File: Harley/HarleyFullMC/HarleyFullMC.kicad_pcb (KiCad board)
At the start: 10 copper layers, 33 x 45 mm, 214 parts, among them J1 USB_3.1_microB, J3 CONN_01X04, J4 CONN_02X05, J5 DF40C_60DP_0-4V, J6 CONN_01X06, U1 xc7a50tcsg324pkg, U10 LTM4622, U11 OSCILLATOR, U12 24LC128T-I/MNY, U2 LTM4622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

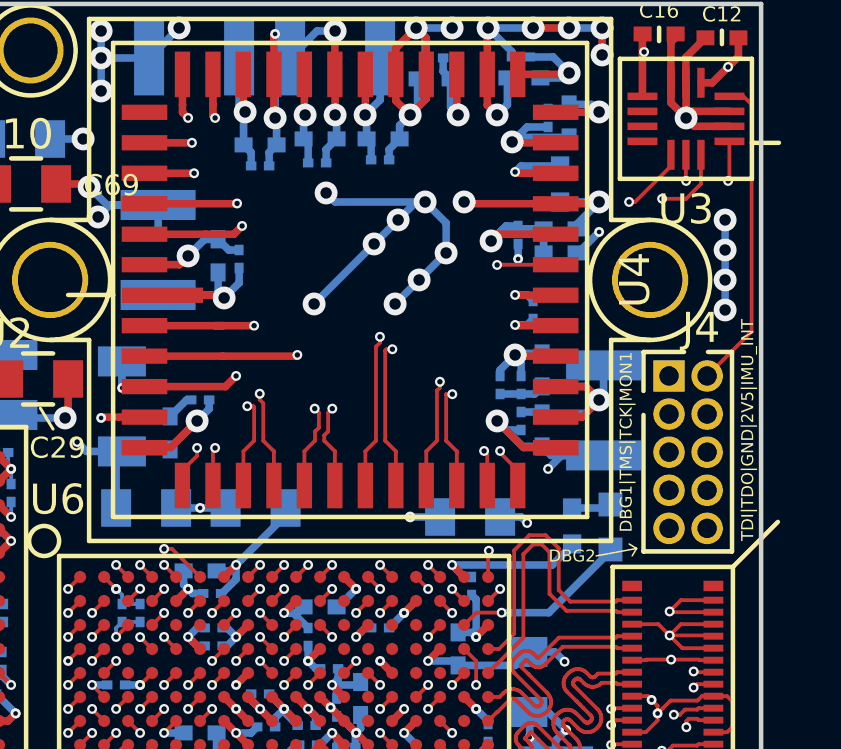
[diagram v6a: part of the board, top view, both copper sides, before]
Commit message: fixed no net vias under imager chip
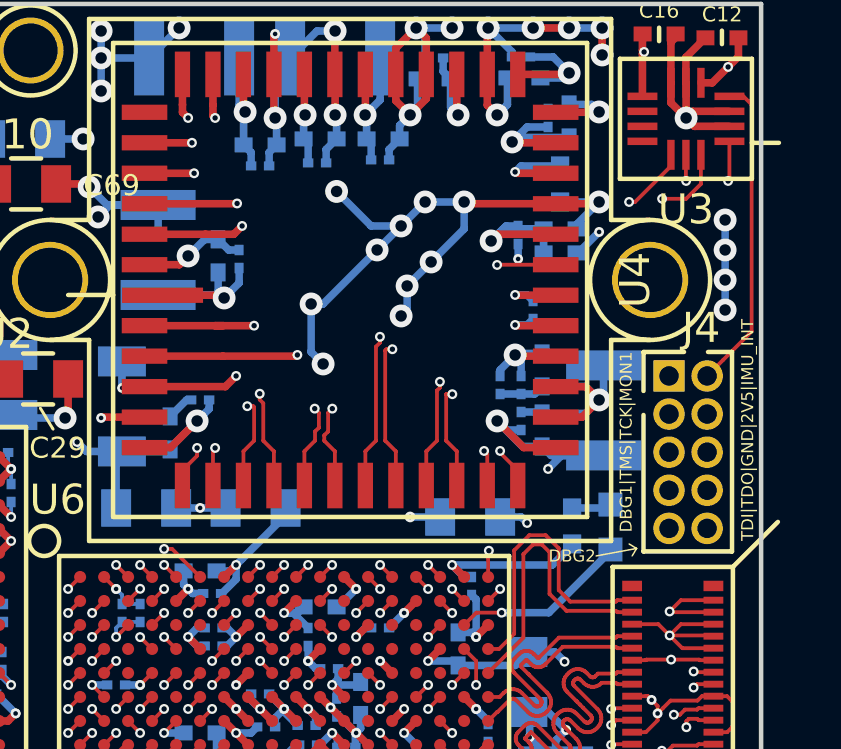
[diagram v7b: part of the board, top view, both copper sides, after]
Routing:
- net GND: track 350.2 -> 366.2 mm, vias 202 -> 211
- net (no net): track 15.9 -> 3.00 mm, vias 14 -> 6
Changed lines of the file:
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@@
     (links 864)
     (no_connects 0)
-    (area 11.924999 152.924999 45.075001 198.075001)
+    (area 8.286961 149.048 50.487715 201.885333)
     (thickness 1.6)
     (drawings 66)
-    (tracks 6054)
+    (tracks 6059)
     (zones 0)
     (modules 214)
@@
   (page A4)
   (layers
-    (0 F.Cu signal hide)
-    (1 In1.Cu power hide)
-    (2 In2.Cu signal hide)
-    (3 In3.Cu signal hide)
-    (4 In4.Cu power hide)
-    (5 In5.Cu signal hide)
-    (6 In6.Cu power hide)
-    (7 In7.Cu power hide)
-    (8 In8.Cu power hide)
+    (0 F.Cu signal)
+    (1 In1.Cu power)
+    (2 In2.Cu signal)
+    (3 In3.Cu signal)
+    (4 In4.Cu power)
+    (5 In5.Cu signal)
+    (6 In6.Cu power)
+    (7 In7.Cu power)
+    (8 In8.Cu power)
     (31 B.Cu signal)
     (34 B.Paste user hide)
@@
   )
   (setup
-    (last_trace_width 0.127)
+    (last_trace_width 0.254)
     (user_trace_width 0.127)
     (user_trace_width 0.254)
@@
     (tags "capacitor 0402")
     (attr smd)
-    (fp_text reference C10 (at 0 1.4) (layer B.SilkS)
+    (fp_text reference C10 (at -0.3 1.7) (layer B.SilkS)
       (effects (font (size 0.5 0.5) (thickness 0.07)) (justify mirror))
     )
@@
     (tags "capacitor 0201")
     (attr smd)
-    (fp_text reference C32 (at 0.05 1.5) (layer B.SilkS)
+    (fp_text reference C32 (at -0.2 1.7) (layer B.SilkS)
       (effects (font (size 0.5 0.5) (thickness 0.07)) (justify mirror))
     )
@@
     (effects (font (size 0.4 0.4) (thickness 0.06)) (justify mirror))
   )
-  (gr_text 2V5 (at 44.4 166.7 360) (layer B.SilkS)
+  (gr_text 2V5 (at 44.4 166.7) (layer B.SilkS)
     (effects (font (size 0.4 0.4) (thickness 0.06)) (justify mirror))
   )
-  (gr_text GND (at 44.35 168 360) (layer B.SilkS)
+  (gr_text GND (at 44.35 168) (layer B.SilkS)
     (effects (font (size 0.4 0.4) (thickness 0.06)) (justify mirror))
   )
-  (gr_text DBG2 (at 38.7 171.4 360) (layer F.SilkS)
+  (gr_text DBG2 (at 38.7 171.4) (layer F.SilkS)
     (effects (font (size 0.4 0.4) (thickness 0.06)))
   )
@@
   (via (at 43.8 161.2) (size 0.762) (drill 0.381) (layers F.Cu B.Cu) (net 0))
   (via (at 43.8 160.2) (size 0.762) (drill 0.381) (layers F.Cu B.Cu) (net 0))
-  (segment (start 33.8 159.600009) (end 30.800009 159.600009) (width 0.254) (layer B.Cu) (net 0))
-  (segment (start 30.800009 159.600009) (end 30.5 159.3) (width 0.254) (layer B.Cu) (net 0))
-  (via (at 30.5 159.3) (size 0.762) (drill 0.381) (layers F.Cu B.Cu) (net 0))
-  (segment (start 32.1 161) (end 30.1 163) (width 0.254) (layer B.Cu) (net 0))
-  (via (at 30.1 163) (size 0.762) (drill 0.381) (layers F.Cu B.Cu) (net 0))
-  (segment (start 32.9 160.2) (end 32.1 161) (width 0.254) (layer B.Cu) (net 0))
-  (via (at 32.1 161) (size 0.762) (drill 0.381) (layers F.Cu B.Cu) (net 0))
-  (segment (start 33.8 159.600009) (end 33.499991 159.600009) (width 0.254) (layer B.Cu) (net 0))
-  (segment (start 33.499991 159.600009) (end 32.9 160.2) (width 0.254) (layer B.Cu) (net 0))
-  (via (at 32.9 160.2) (size 0.762) (drill 0.381) (layers F.Cu B.Cu) (net 0))
-  (segment (start 34.5 161.3) (end 34.5 160.300009) (width 0.254) (layer B.Cu) (net 0))
-  (segment (start 34.5 160.300009) (end 33.8 159.600009) (width 0.254) (layer B.Cu) (net 0))
-  (via (at 33.8 159.600009) (size 0.762) (drill 0.381) (layers F.Cu B.Cu) (net 0))
-  (segment (start 33.6 162.2) (end 34.5 161.3) (width 0.254) (layer B.Cu) (net 0))
-  (via (at 34.5 161.3) (size 0.762) (drill 0.381) (layers F.Cu B.Cu) (net 0))
-  (segment (start 32.8 163) (end 33.6 162.2) (width 0.254) (layer B.Cu) (net 0))
-  (via (at 33.6 162.2) (size 0.762) (drill 0.381) (layers F.Cu B.Cu) (net 0))
-  (via (at 32.8 163) (size 0.762) (drill 0.381) (layers F.Cu B.Cu) (net 0))
   (via (at 23.5 182.9) (size 0.3302) (drill 0.1778) (layers F.Cu B.Cu) (net 0))
   (via (at 22.7 182.9) (size 0.3302) (drill 0.1778) (layers F.Cu B.Cu) (net 0))
@@
   (segment (start 15.34117 160.75883) (end 14.7 161.4) (width 0.254) (layer F.Cu) (net 1))
   (via (at 14.7 161.4) (size 0.3302) (drill 0.1778) (layers F.Cu B.Cu) (net 1))
+  (segment (start 30 163) (end 30 164.6) (width 0.254) (layer B.Cu) (net 2))
+  (segment (start 30 164.6) (end 30.4 165) (width 0.254) (layer B.Cu) (net 2))
+  (via (at 30.4 165) (size 0.762) (drill 0.381) (layers F.Cu B.Cu) (net 2))
+  (segment (start 32.2 161.2) (end 30.4 163) (width 0.254) (layer B.Cu) (net 2))
+  (segment (start 30.4 163) (end 30 163) (width 0.254) (layer B.Cu) (net 2))
+  (via (at 30 163) (size 0.762) (drill 0.381) (layers F.Cu B.Cu) (net 2))
+  (segment (start 33 160.4) (end 32 160.4) (width 0.254) (layer B.Cu) (net 2))
+  (segment (start 32 160.4) (end 30.849031 159.249031) (width 0.254) (layer B.Cu) (net 2))
+  (via (at 30.849031 159.249031) (size 0.762) (drill 0.381) (layers F.Cu B.Cu) (net 2))
+  (segment (start 33 160.4) (end 32.2 161.2) (width 0.254) (layer B.Cu) (net 2))
+  (via (at 32.2 161.2) (size 0.762) (drill 0.381) (layers F.Cu B.Cu) (net 2))
+  (segment (start 33.8 159.6) (end 33 160.4) (width 0.254) (layer B.Cu) (net 2))
+  (via (at 33 160.4) (size 0.762) (drill 0.381) (layers F.Cu B.Cu) (net 2))
+  (segment (start 35.1 159.6) (end 33.8 159.6) (width 0.254) (layer B.Cu) (net 2))
+  (via (at 33.8 159.6) (size 0.762) (drill 0.381) (layers F.Cu B.Cu) (net 2))
+  (segment (start 33.2 162.4) (end 33.2 163.2) (width 0.254) (layer B.Cu) (net 2))
+  (segment (start 33.2 163.2) (end 33 163.4) (width 0.254) (layer B.Cu) (net 2))
+  (via (at 33 163.4) (size 0.762) (drill 0.381) (layers F.Cu B.Cu) (net 2))
+  (segment (start 34 161.6) (end 33.2 162.4) (width 0.254) (layer B.Cu) (net 2))
+  (via (at 33.2 162.4) (size 0.762) (drill 0.381) (layers F.Cu B.Cu) (net 2))
+  (segment (start 35.1 159.6) (end 35.1 160.5) (width 0.254) (layer B.Cu) (net 2))
+  (segment (start 35.1 160.5) (end 34 161.6) (width 0.254) (layer B.Cu) (net 2))
+  (via (at 34 161.6) (size 0.762) (drill 0.381) (layers F.Cu B.Cu) (net 2))
   (segment (start 31.475 177.775) (end 31.475 177.325) (width 0.254) (layer B.Cu) (net 2))
   (segment (start 31.475 177.325) (end 31.5 177.3) (width 0.254) (layer B.Cu) (net 2))
